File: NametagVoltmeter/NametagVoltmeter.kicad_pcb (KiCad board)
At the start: 4 copper layers, 88.9 x 50.8 mm, 56 parts, among them J1 Conn_01x07_Pin, J11 I_Input, J14 Barrel_Jack, J15 Barrel_Jack, J16 Conn_01x01_Socket, J17 Conn_01x01_Socket, J2 MicoSD, J3 Conn_01x07_Pin, J7 Conn_01x02_Pin, J9 Out to Screen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

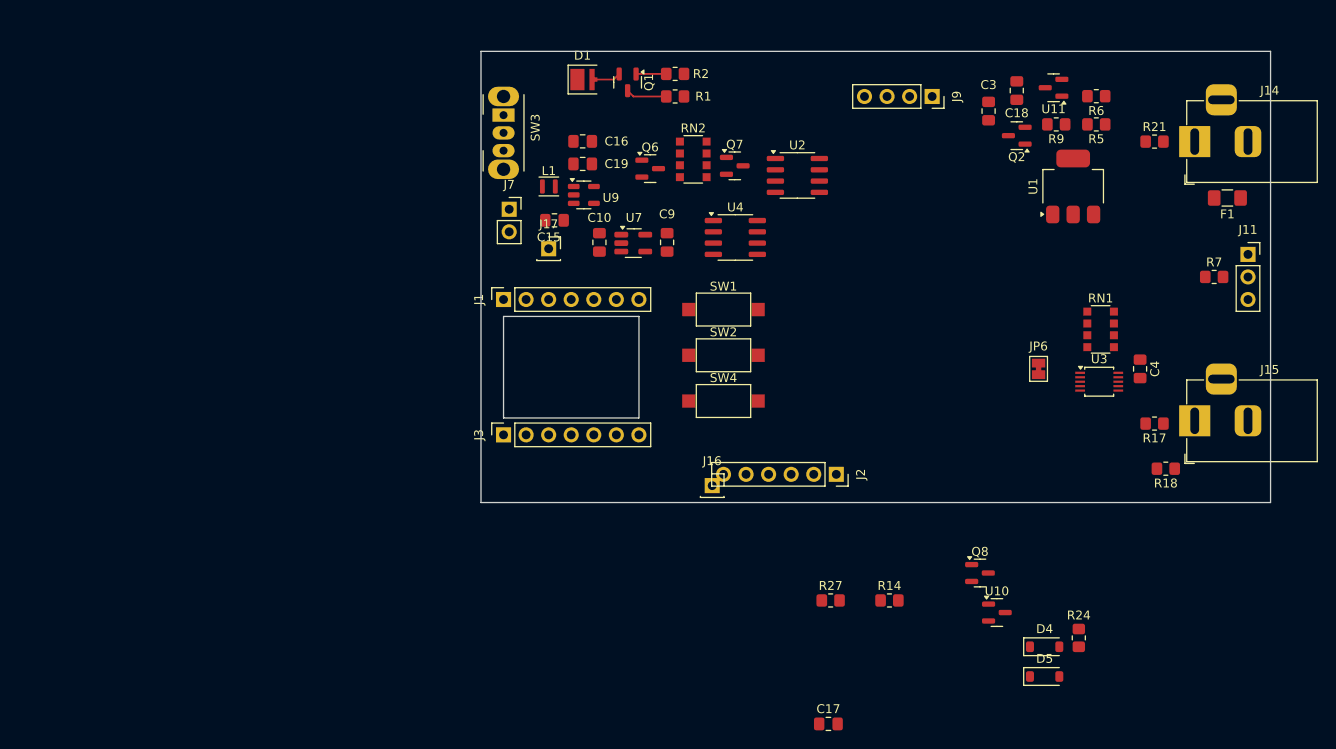
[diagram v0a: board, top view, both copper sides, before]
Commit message: Minor Giga Updates, Working on a business card size version
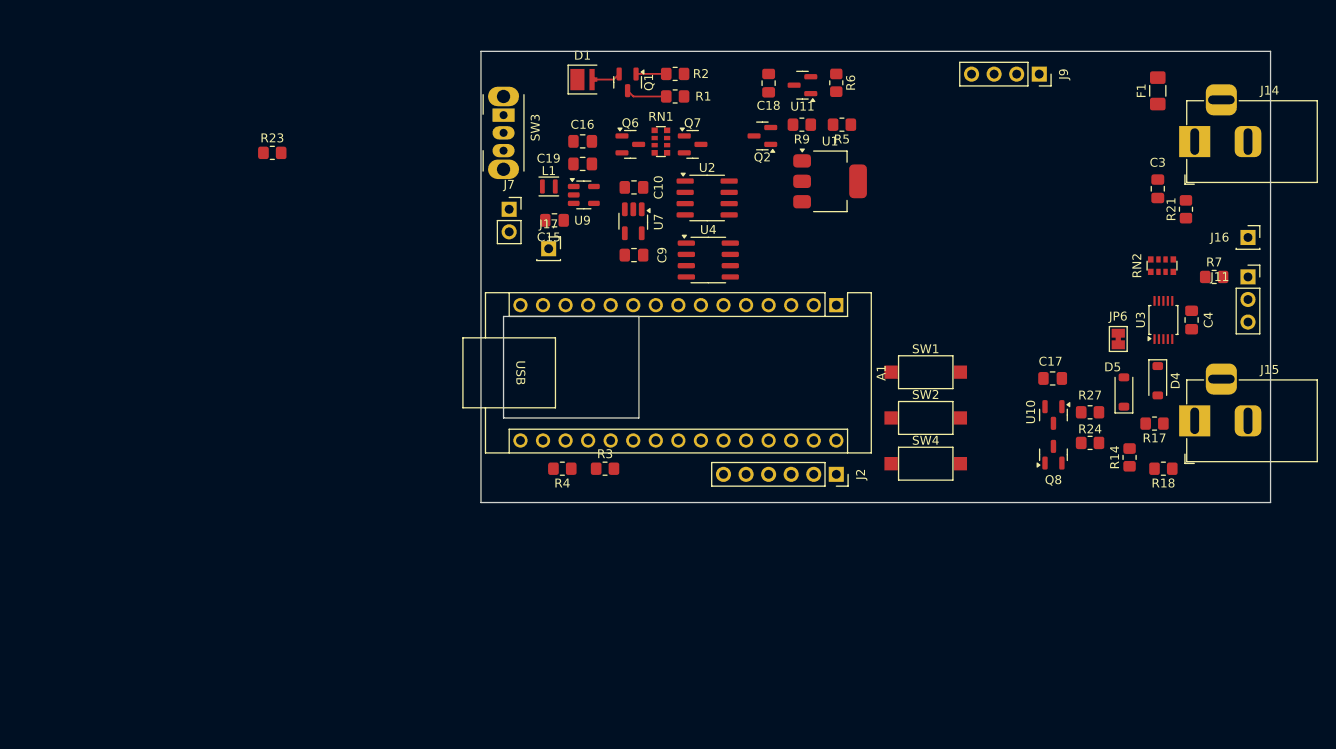
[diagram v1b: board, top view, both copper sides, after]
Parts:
- removed J1, J3: Conn_01x07_Pin, Connector_PinSocket_2.54mm:PinSocket_1x07_P2.54mm_Vertical
- added A1: Arduino_Nano_ESP32, Module:Arduino_Nano, F.Cu at (167.0, 104.8)
- added R23: 0, Resistor_SMD:R_0805_2012Metric_Pad1.20x1.40mm_HandSolder, F.Cu at (103.5, 87.6)
- added R3: 22K, Resistor_SMD:R_0805_2012Metric_Pad1.20x1.40mm_HandSolder, F.Cu at (141.0, 123.2)
- added R4: 100K, Resistor_SMD:R_0805_2012Metric_Pad1.20x1.40mm_HandSolder, F.Cu at (136.2, 123.2)
- RN1, RN2: footprint Resistor_SMD:R_Array_Convex_4x1206 -> Resistor_SMD:R_Array_Convex_4x0612
- moved J16 66.5 mm to (213.4, 97.2)
- moved RN2 54.1 mm to (203.7, 100.3), turned to 90 degrees
- moved RN1 53.8 mm to (147.3, 86.4)
- moved C17 46.4 mm to (191.4, 113.0)
- moved R27 36.1 mm to (195.6, 116.8), turned to 180 degrees
- moved D5 33.3 mm to (199.4, 114.6), turned to 90 degrees
- moved D4 32.5 mm to (203.2, 113.3), turned to -90 degrees
- moved R14 31.5 mm to (200.0, 121.9), turned to 90 degrees
- moved R6 29.3 mm to (167.0, 79.7), turned to -90 degrees
- moved R5 28.6 mm to (167.6, 84.5)
- moved R9 28.6 mm to (163.1, 84.5)
- moved Q2 28.6 mm to (158.7, 85.7)
- moved U11 28.3 mm to (163.2, 80.0)
- moved C18 28.0 mm to (159.4, 79.8)
- moved U1 27.4 mm to (166.3, 90.8), turned to 0 degrees
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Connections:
- Q8 pad 2: /ADC-1 -> Net-(Q8-S)
- R14 pad 1: /V Ref to ADS-0 -> Net-(Q8-S)

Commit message: Working on next PCB, mostly.
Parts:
- added C1: 1uF, Capacitor_SMD:C_0805_2012Metric_Pad1.18x1.45mm_HandSolder, F.Cu at (102.9, 99.1)
- added C2: 4.7uF, Capacitor_SMD:C_0805_2012Metric_Pad1.18x1.45mm_HandSolder, F.Cu at (102.9, 107.3)
- added C5: 1uF, Capacitor_SMD:C_0805_2012Metric_Pad1.18x1.45mm_HandSolder, F.Cu at (102.9, 95.9)
- added C6: 1uF, Capacitor_SMD:C_0805_2012Metric_Pad1.18x1.45mm_HandSolder, F.Cu at (102.9, 92.7)
- added L2: 22uH, Inductor_SMD:L_Murata_DFE201610P, F.Cu at (98.4, 101.6)
- added R10: 71.5k, Resistor_SMD:R_0805_2012Metric_Pad1.20x1.40mm_HandSolder, F.Cu at (97.2, 106.0)
- added R8: 732k, Resistor_SMD:R_0805_2012Metric_Pad1.20x1.40mm_HandSolder, F.Cu at (98.4, 110.5)
- added U5: TLV61046ADBVR, Package_TO_SOT_SMD:SOT-23-6_Handsoldering, F.Cu at (102.9, 103.8)
- moved U7 63.6 mm to (81.0, 88.2)
- moved C10 63.6 mm to (81.0, 84.4)
- moved C9 63.6 mm to (81.0, 92.0)
- moved RN2 58.1 mm to (147.3, 86.6), turned to 0 degrees
- moved RN1 57.8 mm to (203.2, 101.0), turned to 90 degrees
- moved U4 41.5 mm to (187.3, 122.6)
- moved R3 22.9 mm to (163.8, 123.8)
- moved R4 22.9 mm to (159.0, 123.8)
- moved R23 16.2 mm to (119.7, 87.0)
- moved J2 15.2 mm to (151.8, 123.8)
- moved J7 14.0 mm to (130.2, 80.0), turned to 90 degrees
- moved C17 4.72 mm to (194.5, 109.5)
- moved U10 4.72 mm to (194.6, 113.7)
- moved J17 4.62 mm to (130.2, 99.7)
- moved SW3 3.52 mm to (129.5, 86.9)
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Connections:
- A1 pad 10: unconnected-(A1-D7-Pad10) -> D7
- A1 pad 11: unconnected-(A1-D8-Pad11) -> CS
- A1 pad 12: unconnected-(A1-D9-Pad12) -> D9~
- A1 pad 13: unconnected-(A1-D10/CS-Pad13) -> D10~
- A1 pad 14: unconnected-(A1-D11/COPI-Pad14) -> MOSI
- A1 pad 15: unconnected-(A1-D12/CIPO-Pad15) -> MISO
- A1 pad 16: unconnected-(A1-D13/SCK-Pad16) -> CLK
- A1 pad 17: unconnected-(A1-3V3-Pad17) -> +3V3
- A1 pad 19: unconnected-(A1-A0-Pad19) -> A0/D14
- A1 pad 20: unconnected-(A1-A1-Pad20) -> A1/D15
- A1 pad 21: unconnected-(A1-A2-Pad21) -> A2/D16
- A1 pad 23: unconnected-(A1-SDA/A4-Pad23) -> SDA
- A1 pad 24: unconnected-(A1-SCL/A5-Pad24) -> SCL
- A1 pad 29: Net-(A1-GND-Pad29) -> GND
- A1 pad 4: Net-(A1-GND-Pad29) -> GND
- A1 pad 6: unconnected-(A1-D3-Pad6) -> D3~
- A1 pad 8: unconnected-(A1-D5-Pad8) -> D5~ (IR)
- A1 pad 9: unconnected-(A1-D6-Pad9) -> D6~
- RN1 pad 2: SDA-5V -> SCL-5V
- RN1 pad 3: SCL-5V -> SDA-5V
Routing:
- net VDD: track 0.00 -> 118.0 mm, vias 0 -> 3
- net SDA-5V: track 0.00 -> 79.9 mm, vias 0 -> 1
- net SCL-5V: track 0.00 -> 73.9 mm, vias 0 -> 3
- net +9V: track 0.00 -> 66.3 mm, vias 0 -> 3
- net Resistor_Input: track 0.00 -> 59.9 mm, vias 0 -> 4
- net GND: track 0.00 -> 53.1 mm, vias 0 -> 14
- net /V Ref to ADS-0: track 0.00 -> 33.8 mm
- net /R Circuit I Output: track 0.00 -> 23.3 mm
- net /ADC-1: track 0.00 -> 21.9 mm
- net +3V3: track 0.00 -> 19.1 mm, vias 0 -> 3
- net /R into ADS: track 0.00 -> 17.9 mm, vias 0 -> 2
- net XIAO Batt Pin: track 0.00 -> 15.9 mm
- net Net-(U1-VO): track 0.00 -> 13.0 mm
- net Net-(F1-Pad1): track 0.00 -> 11.9 mm
- net V_Input_REF: track 0.00 -> 10.8 mm
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- added copper zone on F.Cu, net GND
- added copper zone on F.Cu, net VDD
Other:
- outline, holes or cut-outs redrawn
- board text added: "The Business Card Voltmeter +/- 50VDC Max"

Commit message: Fixed ammeter problem and some nuisance alerts on Giga version
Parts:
- L2: footprint Inductor_SMD:L_Murata_DFE201610P -> Inductor_SMD:L_Taiyo-Yuden_MD-5050
- moved C10 11.8 mm to (76.6, 95.3)
- moved C9 11.8 mm to (76.6, 103.0)
- moved U7 11.8 mm to (76.5, 99.1)
- moved L2 1.42 mm to (97.2, 101.0)

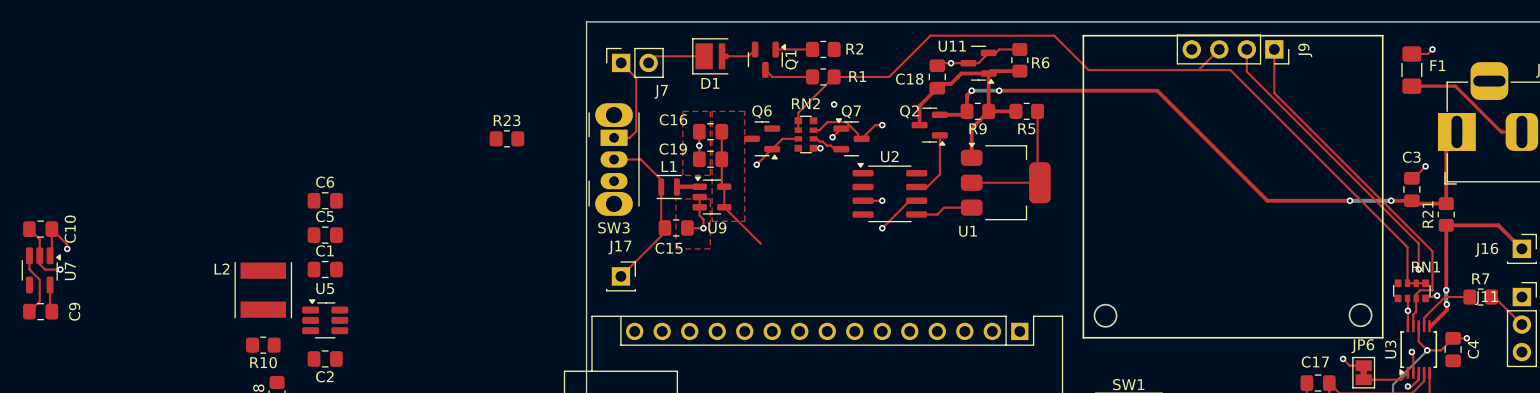
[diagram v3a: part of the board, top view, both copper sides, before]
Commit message: Edits to the RA4M1 version and KiCAD work
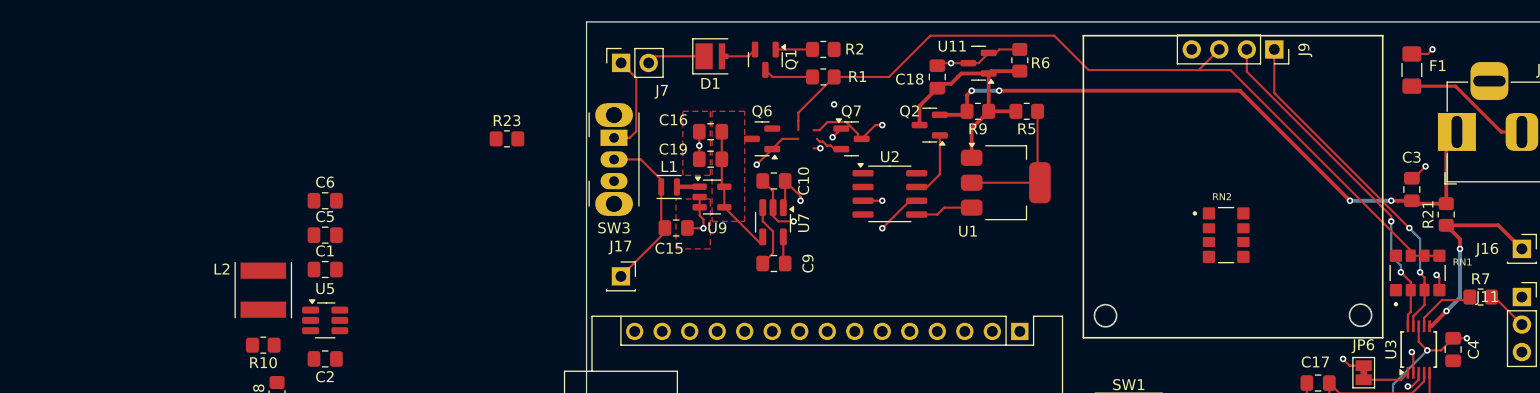
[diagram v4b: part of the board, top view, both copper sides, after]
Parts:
- RN1, RN2: footprint Resistor_SMD:R_Array_Convex_4x0612 -> Library:RESCAXS127P508X320X70-8N
- moved C10 67.8 mm to (144.3, 90.9)
- moved C9 67.8 mm to (144.3, 98.5)
- moved U7 67.8 mm to (144.2, 94.7)
- moved RN2 39.9 mm to (186.1, 95.9)
- moved RN1 1.74 mm to (203.7, 99.4)
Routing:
- net ADS_ALERT: track 9.49 -> 11.5 mm
- net SCL-5V: track 73.9 -> 72.1 mm
- net VDD: track 118.0 -> 116.5 mm
- net +3V3: track 19.1 -> 17.9 mm
- net /R into ADS: track 17.9 -> 19.0 mm
- net SDA-5V: track 79.9 -> 79.2 mm, vias 1 -> 3

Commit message: Minor KiCAD updates and file reorganization
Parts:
- Q2: value SI2302 MOSFET -> AO3400A
- Q8: value SI2302 MOSFET -> AO3400A MOSFET
- moved Q6 53.2 mm to (187.1, 117.2), turned to 90 degrees
- moved L2 49.7 mm to (145.5, 89.4)
- moved C2 49.5 mm to (151.2, 96.8)
- moved R10 49.5 mm to (145.5, 95.5)
- moved U5 49.5 mm to (151.2, 93.2)
- moved R8 49.5 mm to (146.8, 100.0)
- moved C1 49.3 mm to (151.2, 89.4)
- moved C5 49.2 mm to (151.2, 86.9)
- moved C6 49.1 mm to (151.2, 84.3)
- moved Q7 41.4 mm to (187.1, 107.9), turned to 90 degrees
- moved C10 37.0 mm to (111.3, 74.2)
- moved C9 37.0 mm to (111.3, 81.8)
- moved U7 37.0 mm to (111.2, 78.0)
- moved RN2 16.7 mm to (187.1, 112.6), turned to 90 degrees
- moved U2 12.3 mm to (165.4, 98.8), turned to 180 degrees
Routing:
- net +9V: track 66.3 -> 9.69 mm, vias 3 -> 1
- net SDA-5V: track 79.2 -> 57.9 mm, vias 3 -> 2
- net VDD: track 116.5 -> 130.1 mm, vias 3 -> 6
- net SCL-5V: track 72.1 -> 61.5 mm, vias 3 -> 4
- net Net-(Q2-G): track 6.22 -> 0.00 mm
- net /Driver_U2_Out_B: track 5.34 -> 0.00 mm
- net GND: track 53.1 -> 48.2 mm, vias 14 -> 13
- net +3V3: track 17.9 -> 22.6 mm, vias 3 -> 2
- net SCL: track 0.00 -> 4.36 mm
- net Net-(U7-C1-): track 5.95 -> 4.69 mm
